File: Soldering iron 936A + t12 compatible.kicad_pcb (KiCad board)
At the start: 2 copper layers, 97 x 67 mm, 112 parts, among them J1 DC INPUT, J2 USB TO SERIAL, J3 AC input, J4 output_connector, J5 mosfet_driver_future_backup, J6 OLED, J7 USB C BREAKOUT BOARD, Q1 IRF9540N, Q2 BC547, SW1 RotaryEncoder_Switch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

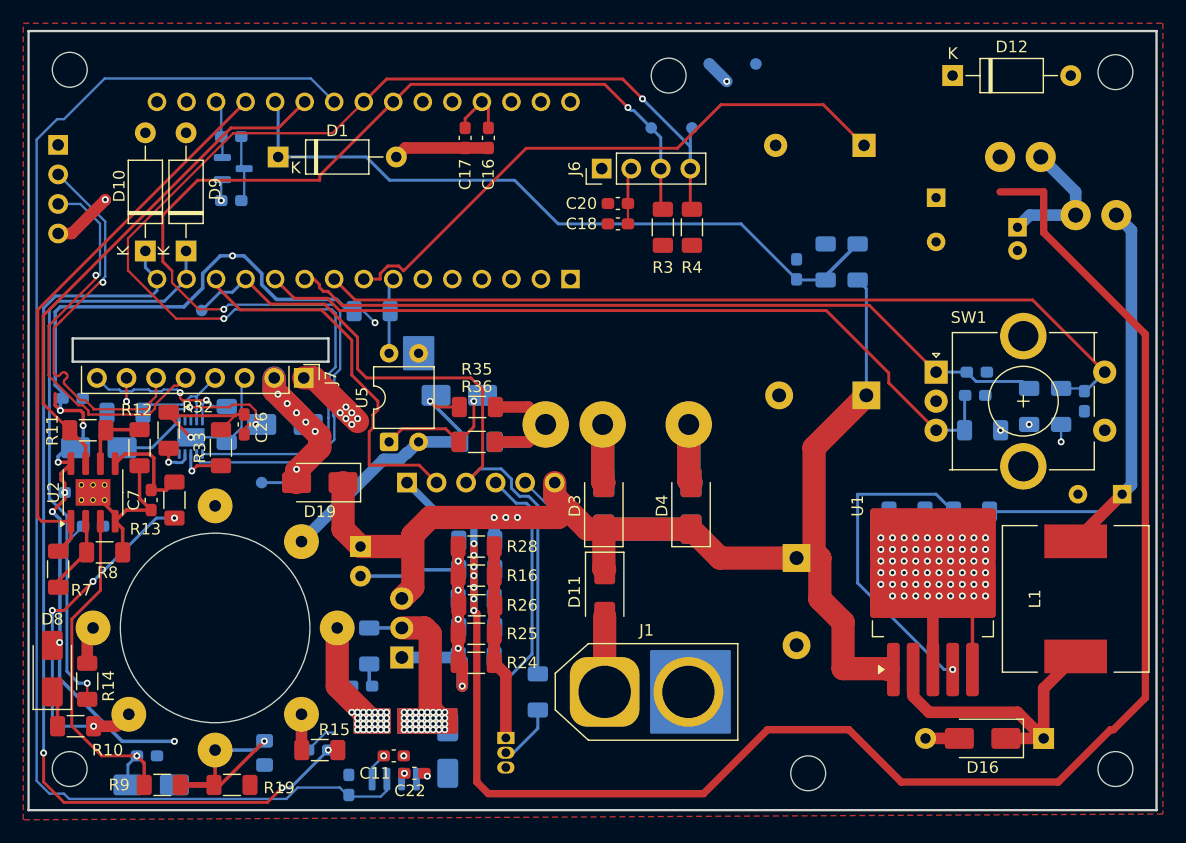
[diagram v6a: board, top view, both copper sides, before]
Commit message: widened the slots
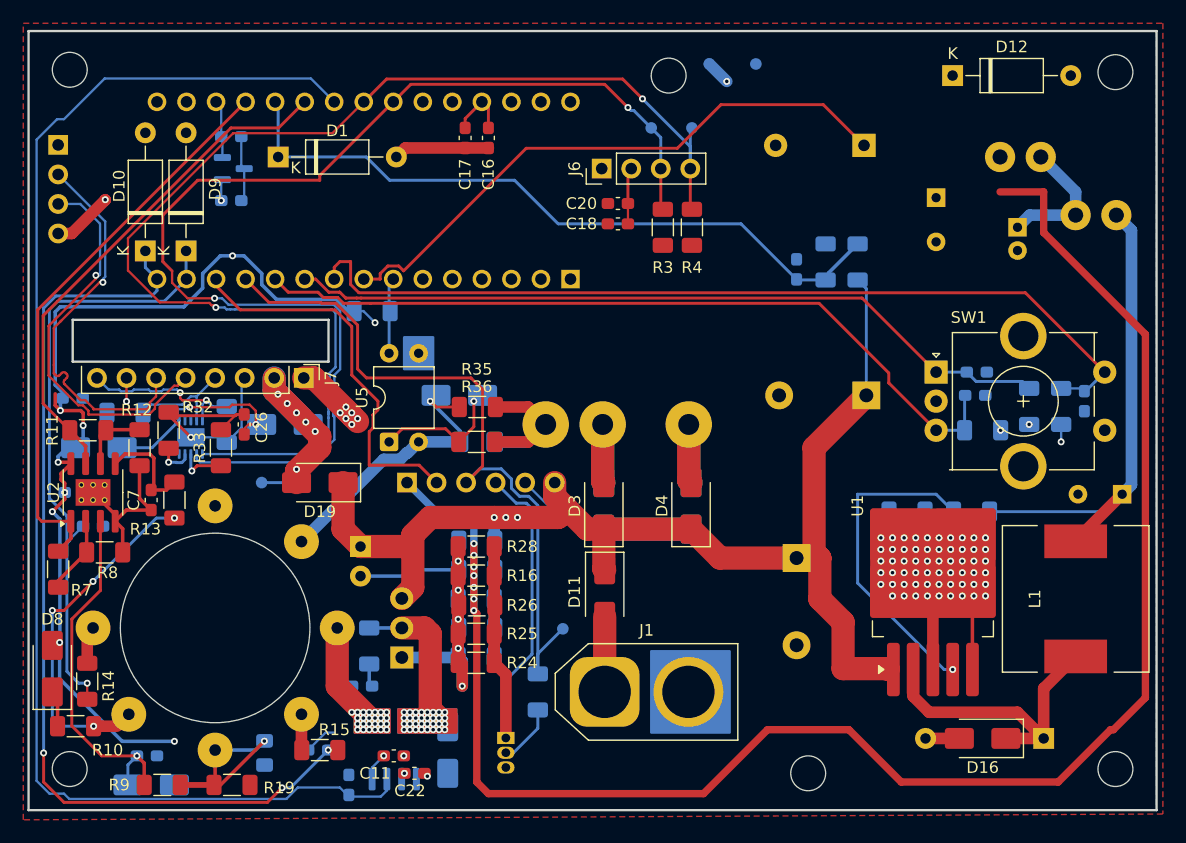
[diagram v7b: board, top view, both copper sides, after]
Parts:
- moved PWM1 41.4 mm to (216.9, 117.6)
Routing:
- net /ENCODER S: track 74.4 -> 77.3 mm
- net /PWM1: track 32.6 -> 33.3 mm
- net /SDA: track 110.7 -> 110.0 mm
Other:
- outline, holes or cut-outs redrawn

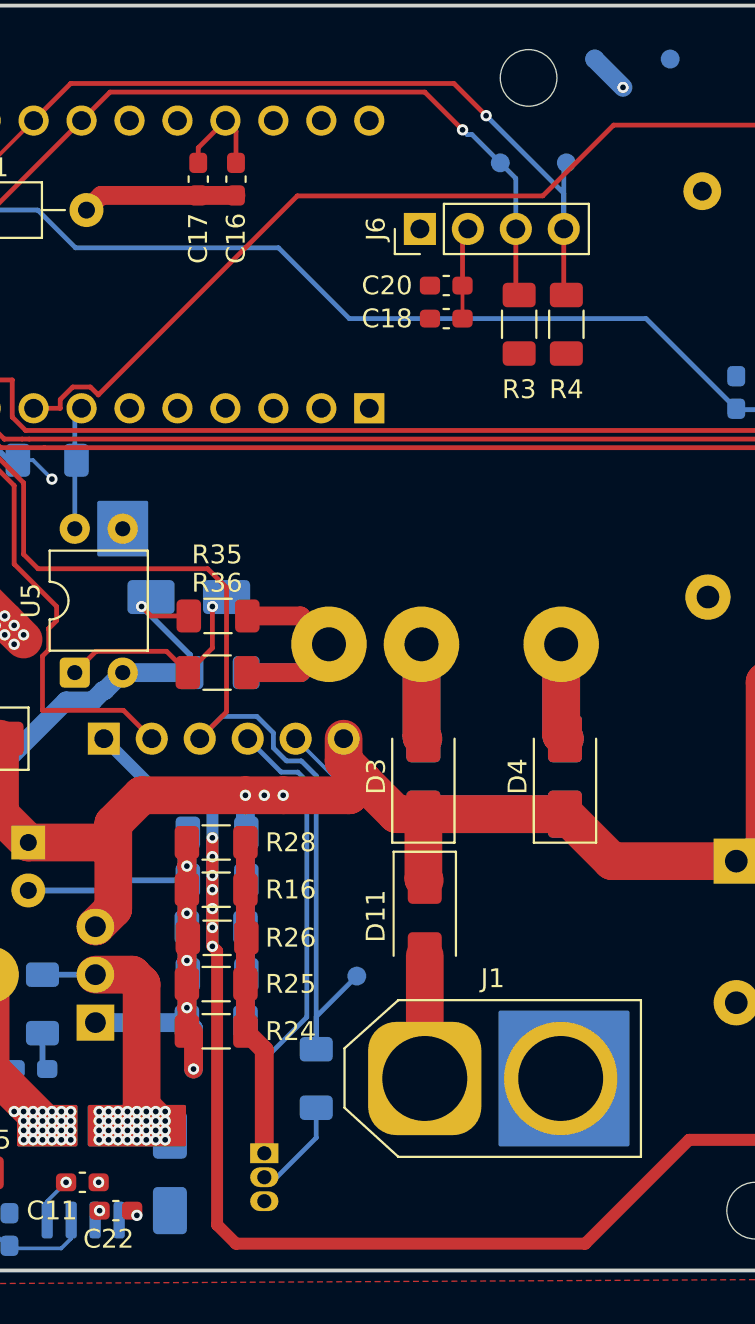
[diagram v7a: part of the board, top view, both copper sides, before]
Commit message: Centralised the connector and screen
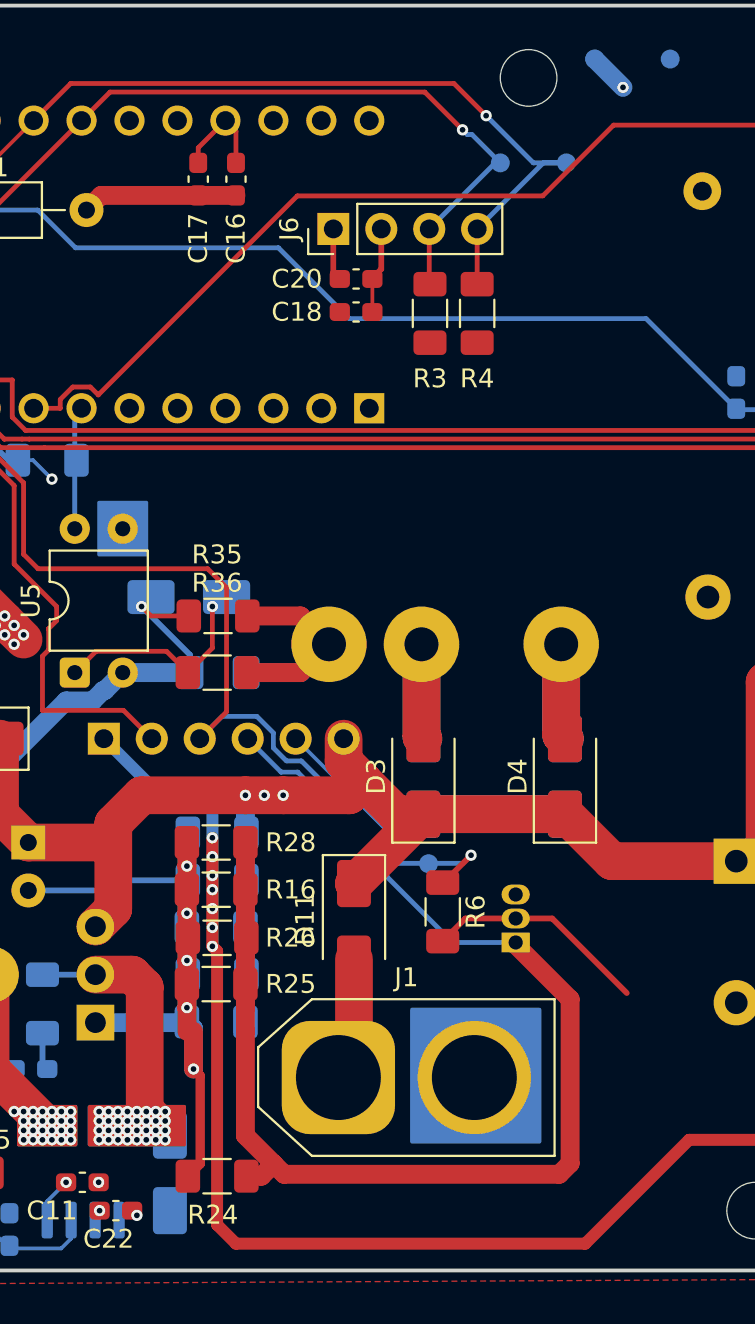
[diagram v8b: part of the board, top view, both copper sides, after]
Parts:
- R6: moved to F.Cu
- moved Q2 17.4 mm to (225.3, 115.8), turned to 90 degrees
- moved R6 11.1 mm to (221.4, 114.2)
- moved R24 7.68 mm to (209.5, 128.2)
- moved PWM1 7.06 mm to (220.7, 111.6)
- moved C18 4.79 mm to (216.9, 82.4)
- moved C20 4.79 mm to (216.9, 80.7)
- moved R3 4.76 mm to (220.8, 82.5)
- moved R4 4.76 mm to (223.3, 82.5)
- moved J6 4.59 mm to (215.7, 78.0)
- moved J1 4.58 mm to (215.9, 123.0)
- moved D11 3.75 mm to (216.8, 114.7)
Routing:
- net Net-(J5-Pin_4): track 42.2 -> 68.9 mm
- net Net-(D13-A): track 38.2 -> 44.3 mm
- net Net-(Q2-B): track 5.81 -> 11.9 mm
- net /PWM: track 62.8 -> 57.2 mm, vias 0 -> 1
- net +5V: track 249.5 -> 252.3 mm
- net GND: track 107.6 -> 105.7 mm
- net /VIN: track 116.1 -> 117.7 mm
- net /SCL: track 102.0 -> 103.3 mm
